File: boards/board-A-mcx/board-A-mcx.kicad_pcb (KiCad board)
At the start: 4 copper layers, 74.8 x 157.1 mm, 30 parts, among them J5 SAMTEC_QSE-040-01-X-D-A, K0 Samtec_MCX-J-P-H-ST-TH1, K1 Samtec_MCX-J-P-H-ST-TH1, K10 Samtec_MCX-J-P-H-ST-TH1, K11 Samtec_MCX-J-P-H-ST-TH1, K12 Samtec_MCX-J-P-H-ST-TH1, K13 Samtec_MCX-J-P-H-ST-TH1, K14 Samtec_MCX-J-P-H-ST-TH1, K15 Samtec_MCX-J-P-H-ST-TH1, K16 Samtec_MCX-J-P-H-ST-TH1, K17 Samtec_MCX-J-P-H-ST-TH1, K18 Samtec_MCX-J-P-H-ST-TH1, K19 Samtec_MCX-J-P-H-ST-TH1, K2 Samtec_MCX-J-P-H-ST-TH1, K20 Samtec_MCX-J-P-H-ST-TH1, K21 Samtec_MCX-J-P-H-ST-TH1, K22 Samtec_MCX-J-P-H-ST-TH1, K23 Samtec_MCX-J-P-H-ST-TH1, K3 Samtec_MCX-J-P-H-ST-TH1, K4 Samtec_MCX-J-P-H-ST-TH1, K5 Samtec_MCX-J-P-H-ST-TH1, K6 Samtec_MCX-J-P-H-ST-TH1, K7 Samtec_MCX-J-P-H-ST-TH1, K8 Samtec_MCX-J-P-H-ST-TH1, K9 Samtec_MCX-J-P-H-ST-TH1

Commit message: update after engineering review
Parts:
- removed IV, K0, K1, K10, K11, K12, K13, K14, K15, K16, K17, K18, K19, K2, K20, K21, K22, K23, K3, K4, K5, K6, K7, K8, K9: Samtec_MCX-J-P-H-ST-TH1, Samtec_MCX-J-P-H-ST-TH1
- added J10: Samtec_MCX-J-P-H-ST-TH1, Samtec_MCX-J-P-H-ST-TH1, F.Cu at (75.3, 112.5)
- added J11: Samtec_MCX-J-P-H-ST-TH1, Samtec_MCX-J-P-H-ST-TH1, F.Cu at (75.3, 120.5)
- added J12: Samtec_MCX-J-P-H-ST-TH1, Samtec_MCX-J-P-H-ST-TH1, F.Cu at (17.5, 108.5)
- added J13: Samtec_MCX-J-P-H-ST-TH1, Samtec_MCX-J-P-H-ST-TH1, F.Cu at (17.5, 116.5)
- added J14: Samtec_MCX-J-P-H-ST-TH1, Samtec_MCX-J-P-H-ST-TH1, F.Cu at (17.5, 100.5)
- added J15: Samtec_MCX-J-P-H-ST-TH1, Samtec_MCX-J-P-H-ST-TH1, F.Cu at (17.5, 92.5)
- added J16: Samtec_MCX-J-P-H-ST-TH1, Samtec_MCX-J-P-H-ST-TH1, F.Cu at (17.5, 84.5)
- added J17: Samtec_MCX-J-P-H-ST-TH1, Samtec_MCX-J-P-H-ST-TH1, F.Cu at (17.5, 76.5)
- added J18: Samtec_MCX-J-P-H-ST-TH1, Samtec_MCX-J-P-H-ST-TH1, F.Cu at (17.5, 68.5)
- added J19: Samtec_MCX-J-P-H-ST-TH1, Samtec_MCX-J-P-H-ST-TH1, F.Cu at (17.5, 60.5)
- added J20: Samtec_MCX-J-P-H-ST-TH1, Samtec_MCX-J-P-H-ST-TH1, F.Cu at (17.5, 52.5)
- added J21: Samtec_MCX-J-P-H-ST-TH1, Samtec_MCX-J-P-H-ST-TH1, F.Cu at (17.5, 44.5)
- added J22: Samtec_MCX-J-P-H-ST-TH1, Samtec_MCX-J-P-H-ST-TH1, F.Cu at (17.5, 28.5)
- added J23: Samtec_MCX-J-P-H-ST-TH1, Samtec_MCX-J-P-H-ST-TH1, F.Cu at (17.5, 36.5)
- added J24: Samtec_MCX-J-P-H-ST-TH1, Samtec_MCX-J-P-H-ST-TH1, F.Cu at (75.3, 24.5)
- added J25: Samtec_MCX-J-P-H-ST-TH1, Samtec_MCX-J-P-H-ST-TH1, F.Cu at (75.3, 32.5)
- added J26: Samtec_MCX-J-P-H-ST-TH1, Samtec_MCX-J-P-H-ST-TH1, F.Cu at (75.3, 40.5)
- added J27: Samtec_MCX-J-P-H-ST-TH1, Samtec_MCX-J-P-H-ST-TH1, F.Cu at (75.3, 48.5)
- added J28: Samtec_MCX-J-P-H-ST-TH1, Samtec_MCX-J-P-H-ST-TH1, F.Cu at (75.3, 56.5)
- added J29: Samtec_MCX-J-P-H-ST-TH1, Samtec_MCX-J-P-H-ST-TH1, F.Cu at (75.3, 64.5)
- added J30: Samtec_MCX-J-P-H-ST-TH1, Samtec_MCX-J-P-H-ST-TH1, F.Cu at (75.3, 72.5)
- added J6: Samtec_MCX-J-P-H-ST-TH1, Samtec_MCX-J-P-H-ST-TH1, F.Cu at (75.3, 80.5)
- added J7: Samtec_MCX-J-P-H-ST-TH1, Samtec_MCX-J-P-H-ST-TH1, F.Cu at (75.3, 88.5)
- added J8: Samtec_MCX-J-P-H-ST-TH1, Samtec_MCX-J-P-H-ST-TH1, F.Cu at (75.3, 96.5)
- added J9: Samtec_MCX-J-P-H-ST-TH1, Samtec_MCX-J-P-H-ST-TH1, F.Cu at (75.3, 104.5)
- moved MH3 32.0 mm to (17.5, 130.1)
- moved MH4 32.0 mm to (75.3, 130.1)
- moved J5 16.0 mm to (46.4, 72.5)
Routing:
- net SIPM_K5: track 84.3 -> 46.4 mm
- net SIPM_K18: track 82.8 -> 45.9 mm
- net SIPM_K16: track 58.7 -> 43.3 mm
- net SIPM_K7: track 57.8 -> 43.3 mm
- net SIPM_K6: track 52.7 -> 40.4 mm
- net SIPM_K17: track 52.3 -> 40.4 mm
- net SIPM_K19: track 39.4 -> 40.0 mm
- net SIPM_K4: track 39.5 -> 40.0 mm
- net GNDA: vias 303 -> 191
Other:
- board size 74.8 x 157.1 mm -> 74.8 x 125.1 mm
- board text added: "IV"
- board text added: "K0"
- board text added: "K1"
- board text added: "K10"
- board text added: "K11"
- board text added: "K12"
- board text added: "K13"
- board text added: "K14"
- board text added: "K15"
- board text added: "K16"
- board text added: "K17"
- board text added: "K18"
- board text added: "K19"
- board text added: "K2"
- board text added: "K20"
- board text added: "K21"
- board text added: "K22"
- board text added: "K23"
- board text added: "K3"
- board text added: "K4"
- board text added: "K5"
- board text added: "K6"
- board text added: "K7"
- board text added: "K8"
- board text added: "K9"

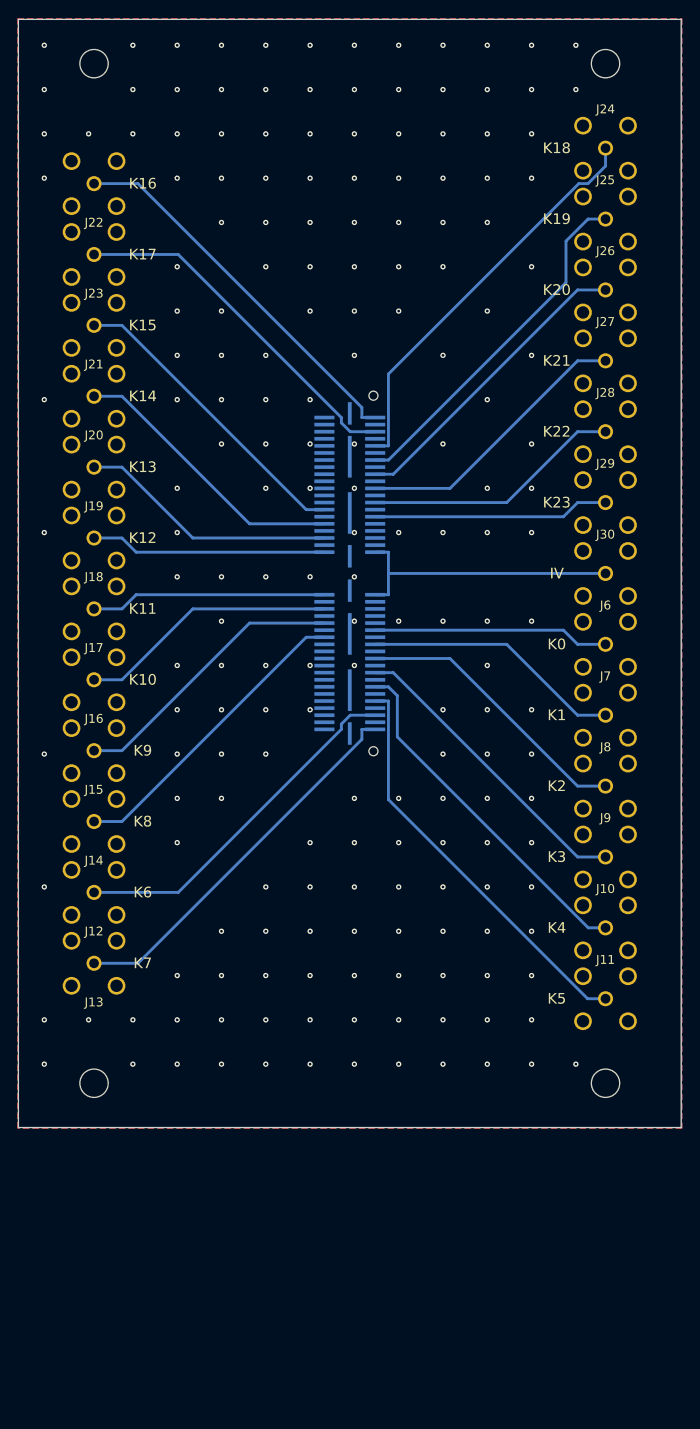
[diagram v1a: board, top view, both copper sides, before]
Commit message: Clean up routing and MCX connector placement.
Adjust silkscreen circuit designator size and placement.
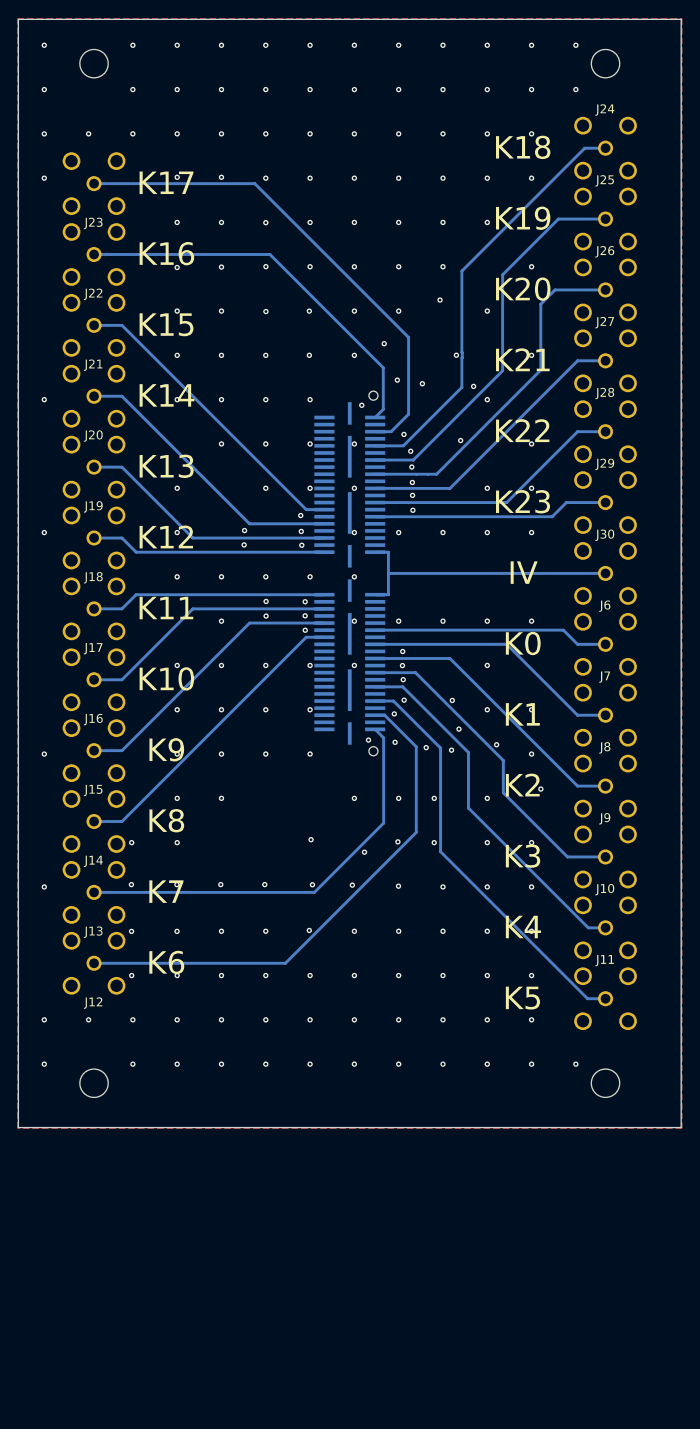
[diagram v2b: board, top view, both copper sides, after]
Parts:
- renumbered J13 to J12, J12 to J13, J23 to J22, J22 to J23
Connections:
- J12 pad 1: SIPM_K7 -> SIPM_K6
- J13 pad 1: SIPM_K6 -> SIPM_K7
- J22 pad 1: SIPM_K17 -> SIPM_K16
- J23 pad 1: SIPM_K16 -> SIPM_K17
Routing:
- net SIPM_K6: track 40.4 -> 58.3 mm
- net SIPM_K17: track 40.4 -> 55.9 mm
- net SIPM_K20: track 34.6 -> 38.9 mm
- net SIPM_K19: track 40.0 -> 43.6 mm
- net SIPM_K7: track 43.3 -> 46.9 mm
- net SIPM_K3: track 34.6 -> 36.8 mm
- net SIPM_K18: track 45.9 -> 47.6 mm
- net SIPM_K4: track 40.0 -> 40.9 mm
- net SIPM_K16: track 43.3 -> 43.9 mm
- net GNDA: vias 191 -> 234
